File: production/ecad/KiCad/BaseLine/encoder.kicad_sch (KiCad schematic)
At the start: 0 parts

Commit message: Level shifting for encoder
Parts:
- added Q1, Q2, Q3: BSS138, Package_TO_SOT_SMD:SOT-23, symbol Transistor_FET:BSS138
- added R10, R5, R6, R7, R8, R9: 10K, symbol Device:R_Small_US
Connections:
- new net: Q3.3 (D), R10.2
- new net: Q2.3 (D), R8.2
- new net: Q1.3 (D), R6.2
- new net 3.3V: Q1.1 (G), Q2.1 (G), Q3.1 (G), R5.1, R7.1, R9.1
- new net 5V: R10.1, R6.1, R8.1
- new net CLK_encoder: Q2.2 (S), R7.2
- new net CS_encoder: Q3.2 (S), R9.2
- new net Encoder_DO: Q1.2 (S), R5.2
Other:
- note added: "Chip select"
- note added: "Clock"
- note added: "DO"
- note added: "connector type?"

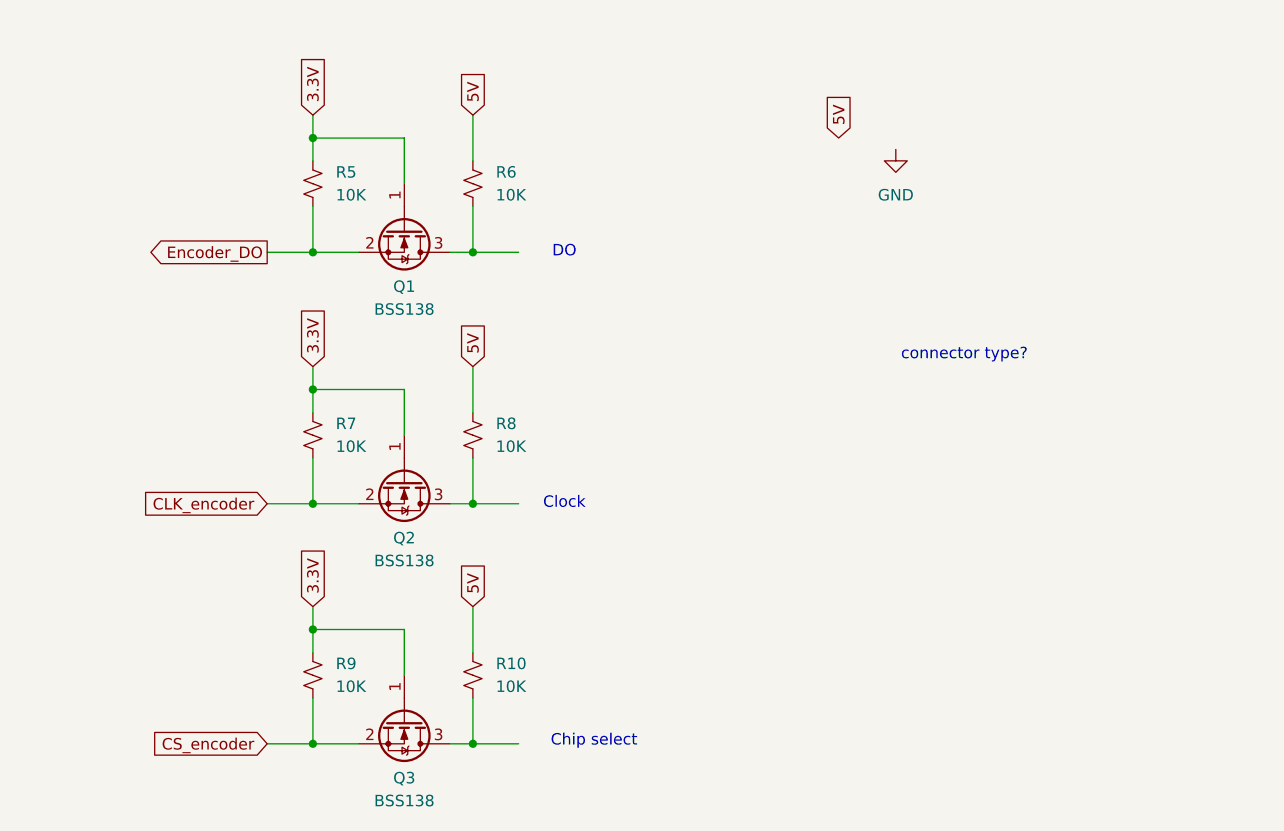
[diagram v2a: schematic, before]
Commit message: wired encoder to connector
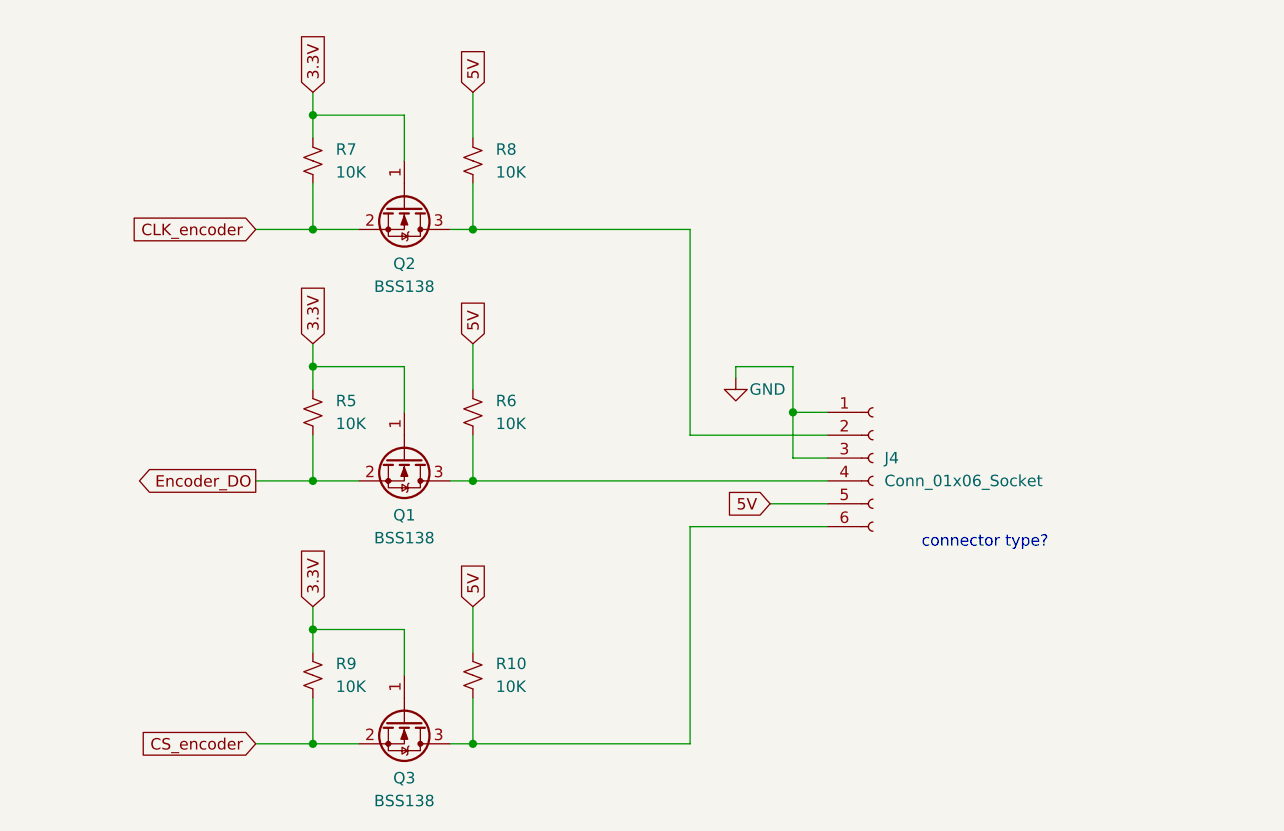
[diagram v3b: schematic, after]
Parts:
- added J4: Conn_01x06_Socket, symbol Connector:Conn_01x06_Socket
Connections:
- net 5V: now also J4.5 (Pin_5)
- net GND: now also J4.1 (Pin_1), J4.3 (Pin_3)
- net at Q3.3 (D), R10.2: now also J4.6 (Pin_6)
- net at Q2.3 (D), R8.2: now also J4.2 (Pin_2)
- net at Q1.3 (D), R6.2: now also J4.4 (Pin_4)
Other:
- note removed: "Chip select"
- note removed: "Clock"
- note removed: "DO"
- moved on the sheet: Q1, Q2, R5, R6, R7, R8

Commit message: replaced lvl shifting rotary encoder
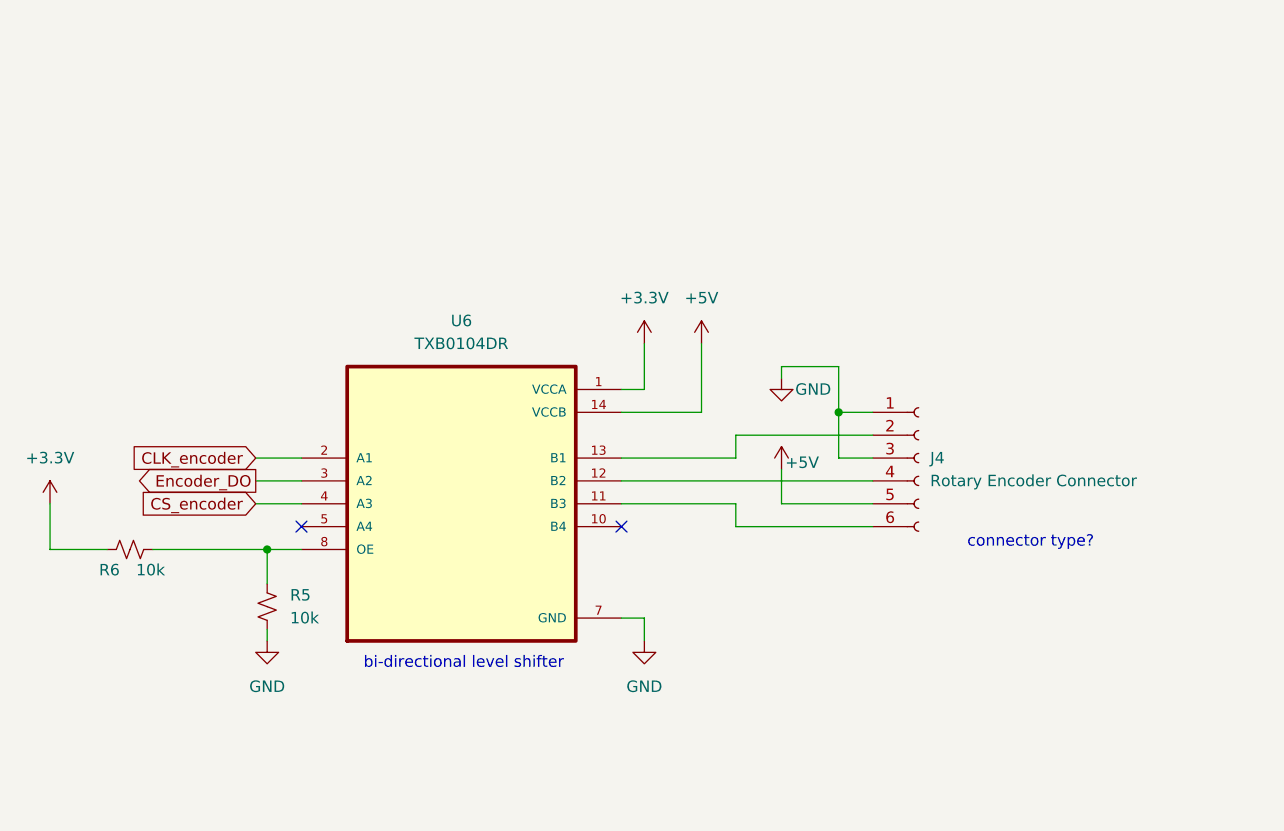
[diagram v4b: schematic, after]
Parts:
- removed Q1, Q2, Q3: BSS138, Package_TO_SOT_SMD:SOT-23, symbol Transistor_FET:BSS138
- removed R10, R7, R8, R9: 10K, symbol Device:R_Small_US
- added U6: TXB0104DR, TXB0104DR:SOIC127P600X175-14N, symbol TXB0104DR:TXB0104DR
- J4: value Conn_01x06_Socket -> Rotary Encoder Connector
- R5, R6: value 10K -> 10k
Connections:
- net 3.3V is gone; now on an unnamed net: R5.1
- net CLK_encoder: now also U6.2 (A1)
- net CS_encoder: now also U6.4 (A3)
- net Encoder_DO: now also U6.3 (A2); no longer R5.2
- net GND: now also R5.2, U6.7 (GND)
- net at J4.6 (Pin_6): now also U6.11 (B3)
- net at J4.2 (Pin_2): now also U6.13 (B1)
- net at R6.2: now also U6.8 (OE); no longer J4.4 (Pin_4)
- net 5V renamed +3.3V
- net +3.3V: now also U6.1 (VCCA); no longer J4.5 (Pin_5)
- new net: J4.4 (Pin_4), U6.12 (B2)
- new net +5V: J4.5 (Pin_5), U6.14 (VCCB)
- no-connect marks 0 -> 2
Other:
- note added: "bi-directional level shifter"
- moved on the sheet: J4

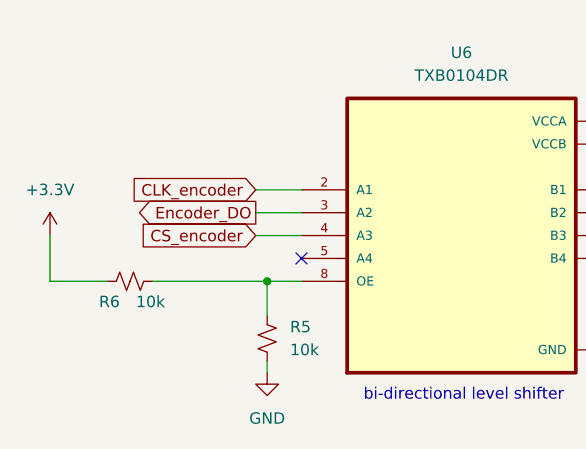
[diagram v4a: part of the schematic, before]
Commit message: MCU connections and matching names
matched the global net names of all the sensor connections with the MCU. Added an IO sheet for the power button
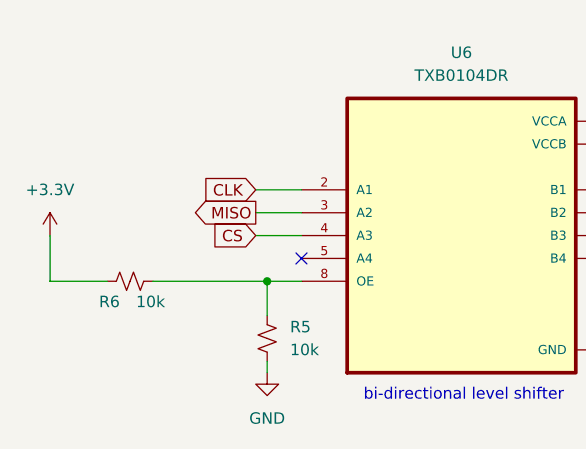
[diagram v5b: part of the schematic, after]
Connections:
- net CLK_encoder renamed CLK
- net CS_encoder renamed CS
- net Encoder_DO renamed MISO
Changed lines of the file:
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@@
 		)
 	)
-	(global_label "Encoder_DO"
+	(global_label "MISO"
 		(shape output)
 		(at 63.5 63.5 180)
@@
 		)
 		(property "Intersheetrefs" "${INTERSHEET_REFS}"
-			(at 49.3873 63.5 0)
+			(at 55.9186 63.5 0)
 			(effects
 				(font
@@
 		)
 	)
-	(global_label "CLK_encoder"
+	(global_label "CLK"
 		(shape input)
 		(at 63.5 60.96 180)
@@
 		)
 		(property "Intersheetrefs" "${INTERSHEET_REFS}"
-			(at 48.4801 60.96 0)
+			(at 56.9467 60.96 0)
 			(effects
 				(font
@@
 		)
 	)
-	(global_label "CS_encoder"
+	(global_label "CS"
 		(shape input)
 		(at 63.5 66.04 180)
@@
 		)
 		(property "Intersheetrefs" "${INTERSHEET_REFS}"
-			(at 49.5687 66.04 0)
+			(at 58.0353 66.04 0)
 			(effects
 				(font

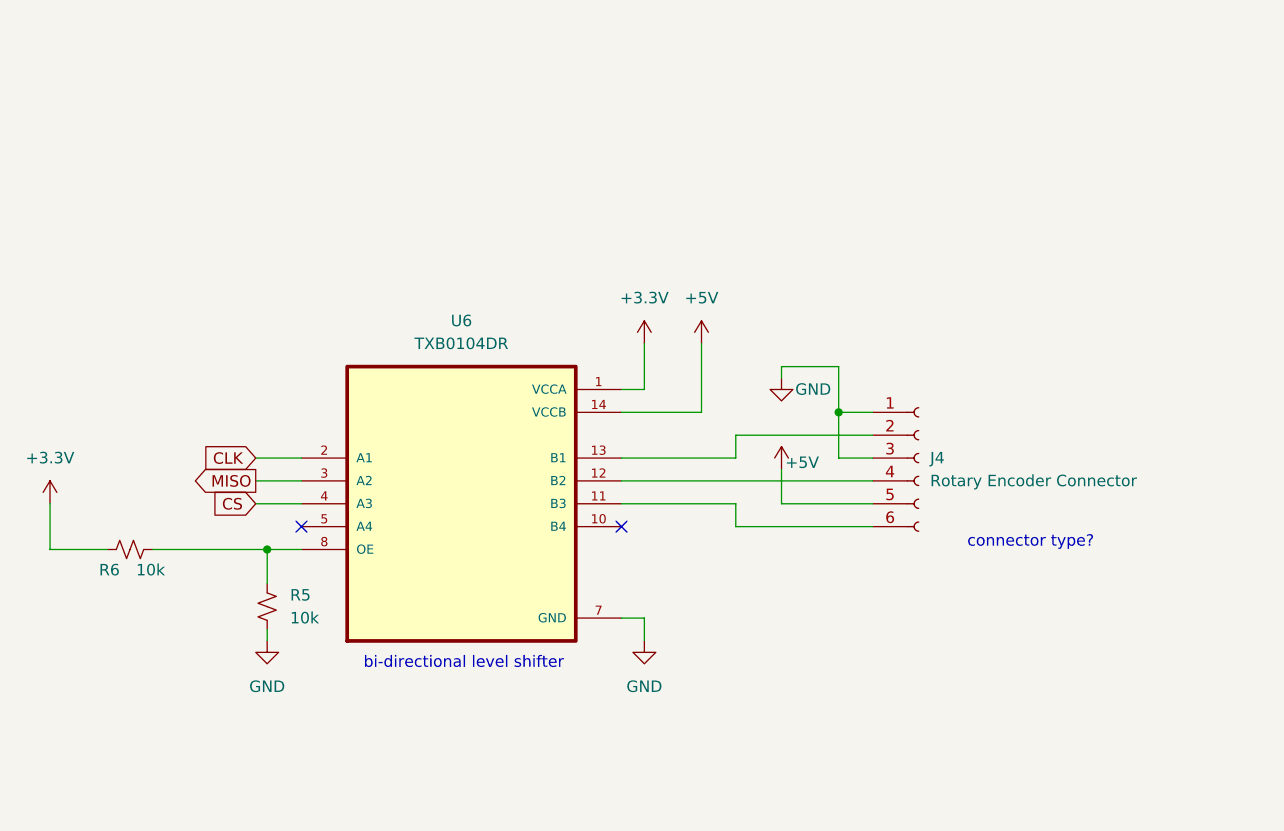
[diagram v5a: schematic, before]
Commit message: testpoints on rotary encoder & IMU
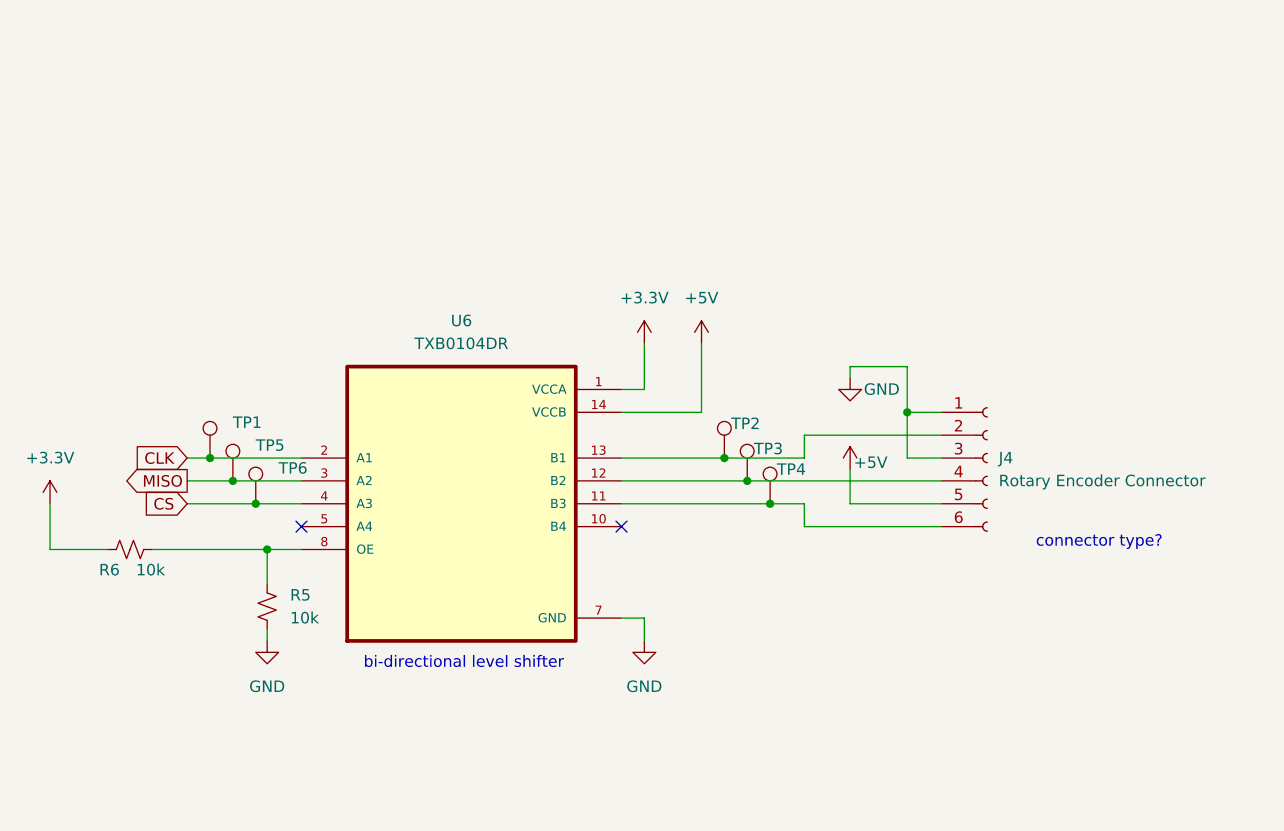
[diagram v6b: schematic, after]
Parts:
- added TP1, TP2, TP3, TP4, TP5, TP6: ~, symbol Connector:TestPoint
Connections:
- net CLK: now also TP1.1
- net CS: now also TP6.1
- net MISO: now also TP5.1
- net at J4.2 (Pin_2), U6.13 (B1): now also TP2.1
- net at J4.4 (Pin_4), U6.12 (B2): now also TP3.1
- net at J4.6 (Pin_6), U6.11 (B3): now also TP4.1
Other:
- moved on the sheet: J4

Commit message: Changed annotations
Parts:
- renumbered J4 to J5, R6 to R36, R5 to R37, TP1 to TP14, TP5 to TP15, TP6 to TP16, TP2 to TP17, TP3 to TP18, TP4 to TP19, U6 to U9
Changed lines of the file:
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@@
 		(on_board yes)
 		(dnp no)
-		(property "Reference" "#PWR049"
+		(property "Reference" "#PWR068"
 			(at 129.54 66.04 0)
 			(effects
@@
 			(project ""
 				(path "/ba9eda21-3882-41e1-8265-3d8ac781da20/83d2619d-438a-45a6-9609-f1b511caf8bd"
-					(reference "#PWR049")
+					(reference "#PWR068")
 					(unit 1)
 				)
@@
 		(dnp no)
 		(fields_autoplaced yes)
-		(property "Reference" "TP6"
+		(property "Reference" "TP16"
 			(at 66.04 62.1029 0)
 			(effects
@@
 			(project "BaseLine"
 				(path "/ba9eda21-3882-41e1-8265-3d8ac781da20/83d2619d-438a-45a6-9609-f1b511caf8bd"
-					(reference "TP6")
+					(reference "TP16")
 					(unit 1)
 				)
@@
 		(dnp no)
 		(fields_autoplaced yes)
-		(property "Reference" "#PWR054"
+		(property "Reference" "#PWR062"
 			(at 40.64 69.85 0)
 			(effects
@@
 			(project ""
 				(path "/ba9eda21-3882-41e1-8265-3d8ac781da20/83d2619d-438a-45a6-9609-f1b511caf8bd"
-					(reference "#PWR054")
+					(reference "#PWR062")
 					(unit 1)
 				)
@@
 		(dnp no)
 		(fields_autoplaced yes)
-		(property "Reference" "TP1"
+		(property "Reference" "TP14"
 			(at 60.96 57.0229 0)
 			(effects
@@
 			(project ""
 				(path "/ba9eda21-3882-41e1-8265-3d8ac781da20/83d2619d-438a-45a6-9609-f1b511caf8bd"
-					(reference "TP1")
+					(reference "TP14")
 					(unit 1)
 				)
@@
 		(dnp no)
 		(fields_autoplaced yes)
-		(property "Reference" "R5"
+		(property "Reference" "R37"
 			(at 67.31 76.1999 0)
 			(effects
@@
 			(project ""
 				(path "/ba9eda21-3882-41e1-8265-3d8ac781da20/83d2619d-438a-45a6-9609-f1b511caf8bd"
-					(reference "R5")
+					(reference "R37")
 					(unit 1)
 				)
@@
 		(dnp no)
 		(fields_autoplaced yes)
-		(property "Reference" "J4"
+		(property "Reference" "J5"
 			(at 146.05 60.9599 0)
 			(effects
@@
 			(project ""
 				(path "/ba9eda21-3882-41e1-8265-3d8ac781da20/83d2619d-438a-45a6-9609-f1b511caf8bd"
-					(reference "J4")
+					(reference "J5")
 					(unit 1)
 				)
@@
 		(dnp no)
 		(fields_autoplaced yes)
-		(property "Reference" "TP5"
+		(property "Reference" "TP15"
 			(at 63.5 59.5629 0)
 			(effects
@@
 			(project "BaseLine"
 				(path "/ba9eda21-3882-41e1-8265-3d8ac781da20/83d2619d-438a-45a6-9609-f1b511caf8bd"
-					(reference "TP5")
+					(reference "TP15")
 					(unit 1)
 				)
@@
 		(dnp no)
 		(fields_autoplaced yes)
-		(property "Reference" "#PWR050"
+		(property "Reference" "#PWR066"
 			(at 113.03 52.07 0)
 			(effects
@@
 			(project ""
 				(path "/ba9eda21-3882-41e1-8265-3d8ac781da20/83d2619d-438a-45a6-9609-f1b511caf8bd"
-					(reference "#PWR050")
+					(reference "#PWR066")
 					(unit 1)
 				)
@@
 		(on_board yes)
 		(dnp no)
-		(property "Reference" "TP4"
+		(property "Reference" "TP19"
 			(at 121.412 62.23 0)
 			(effects
@@
 			(project "BaseLine"
 				(path "/ba9eda21-3882-41e1-8265-3d8ac781da20/83d2619d-438a-45a6-9609-f1b511caf8bd"
-					(reference "TP4")
+					(reference "TP19")
 					(unit 1)
 				)
@@
 		(on_board yes)
 		(dnp no)
-		(property "Reference" "#PWR026"
+		(property "Reference" "#PWR067"
 			(at 129.54 58.42 0)
 			(effects
@@
 			(project ""
 				(path "/ba9eda21-3882-41e1-8265-3d8ac781da20/83d2619d-438a-45a6-9609-f1b511caf8bd"
-					(reference "#PWR026")
+					(reference "#PWR067")
 					(unit 1)
 				)
@@
 		(dnp no)
 		(fields_autoplaced yes)
-		(property "Reference" "#PWR051"
+		(property "Reference" "#PWR064"
 			(at 106.68 52.07 0)
 			(effects
@@
 			(project ""
 				(path "/ba9eda21-3882-41e1-8265-3d8ac781da20/83d2619d-438a-45a6-9609-f1b511caf8bd"
-					(reference "#PWR051")
+					(reference "#PWR064")
 					(unit 1)
 				)
@@
 		(on_board yes)
 		(dnp no)
-		(property "Reference" "TP3"
+		(property "Reference" "TP18"
 			(at 118.872 59.944 0)
 			(effects
@@
 			(project "BaseLine"
 				(path "/ba9eda21-3882-41e1-8265-3d8ac781da20/83d2619d-438a-45a6-9609-f1b511caf8bd"
-					(reference "TP3")
+					(reference "TP18")
 					(unit 1)
 				)
@@
 		(on_board yes)
 		(dnp no)
-		(property "Reference" "R6"
+		(property "Reference" "R36"
 			(at 47.244 73.406 90)
 			(effects
@@
 			(project "BaseLine"
 				(path "/ba9eda21-3882-41e1-8265-3d8ac781da20/83d2619d-438a-45a6-9609-f1b511caf8bd"
-					(reference "R6")
+					(reference "R36")
 					(unit 1)
 				)
@@
 		(dnp no)
 		(fields_autoplaced yes)
-		(property "Reference" "U6"
+		(property "Reference" "U9"
 			(at 86.36 45.72 0)
 			(effects
@@
 			(project ""
 				(path "/ba9eda21-3882-41e1-8265-3d8ac781da20/83d2619d-438a-45a6-9609-f1b511caf8bd"
-					(reference "U6")
+					(reference "U9")
 					(unit 1)
 				)
@@
 		(on_board yes)
 		(dnp no)
-		(property "Reference" "TP2"
+		(property "Reference" "TP17"
 			(at 116.332 57.15 0)
 			(effects
@@
 			(project ""
 				(path "/ba9eda21-3882-41e1-8265-3d8ac781da20/83d2619d-438a-45a6-9609-f1b511caf8bd"
-					(reference "TP2")
+					(reference "TP17")
 					(unit 1)
 				)
@@
 		(dnp no)
 		(fields_autoplaced yes)
-		(property "Reference" "#PWR053"
+		(property "Reference" "#PWR063"
 			(at 64.77 87.63 0)
 			(effects
@@
 			(project "BaseLine"
 				(path "/ba9eda21-3882-41e1-8265-3d8ac781da20/83d2619d-438a-45a6-9609-f1b511caf8bd"
-					(reference "#PWR053")
+					(reference "#PWR063")
 					(unit 1)
 				)
@@
 		(dnp no)
 		(fields_autoplaced yes)
-		(property "Reference" "#PWR052"
+		(property "Reference" "#PWR065"
 			(at 106.68 87.63 0)
 			(effects
@@
 			(project ""
 				(path "/ba9eda21-3882-41e1-8265-3d8ac781da20/83d2619d-438a-45a6-9609-f1b511caf8bd"
-					(reference "#PWR052")
-					(unit 1)
-				)
+					(reference "#PWR065")
+					(unit 1)
+				)

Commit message: More updated annotations and stuff
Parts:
- renumbered R36 to R39, R37 to R40
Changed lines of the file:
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@@
 		(dnp no)
 		(fields_autoplaced yes)
-		(property "Reference" "R37"
+		(property "Reference" "R40"
 			(at 67.31 76.1999 0)
 			(effects
@@
 			(project ""
 				(path "/ba9eda21-3882-41e1-8265-3d8ac781da20/83d2619d-438a-45a6-9609-f1b511caf8bd"
-					(reference "R37")
+					(reference "R40")
 					(unit 1)
 				)
@@
 		(on_board yes)
 		(dnp no)
-		(property "Reference" "R36"
+		(property "Reference" "R39"
 			(at 47.244 73.406 90)
 			(effects
@@
 			(project "BaseLine"
 				(path "/ba9eda21-3882-41e1-8265-3d8ac781da20/83d2619d-438a-45a6-9609-f1b511caf8bd"
-					(reference "R36")
-					(unit 1)
-				)
+					(reference "R39")
+					(unit 1)
+				)
